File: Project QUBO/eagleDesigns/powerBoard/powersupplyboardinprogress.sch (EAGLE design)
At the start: 12 parts, among them M1 IRF7458PBF, M2 IRF7458PBF

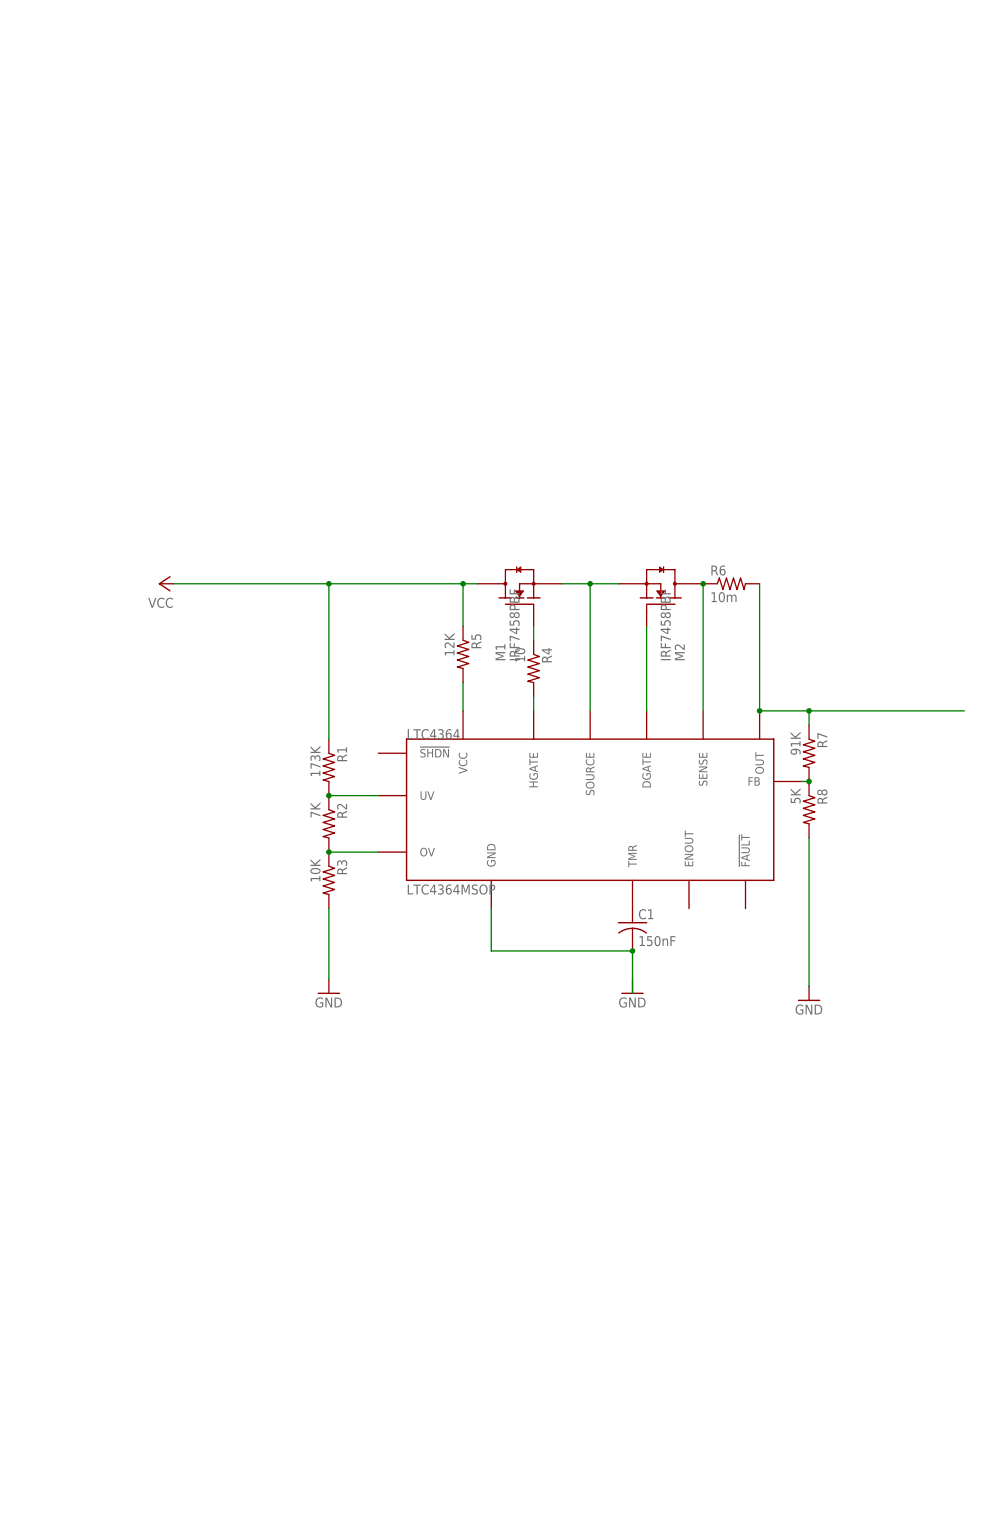
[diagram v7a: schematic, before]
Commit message: 
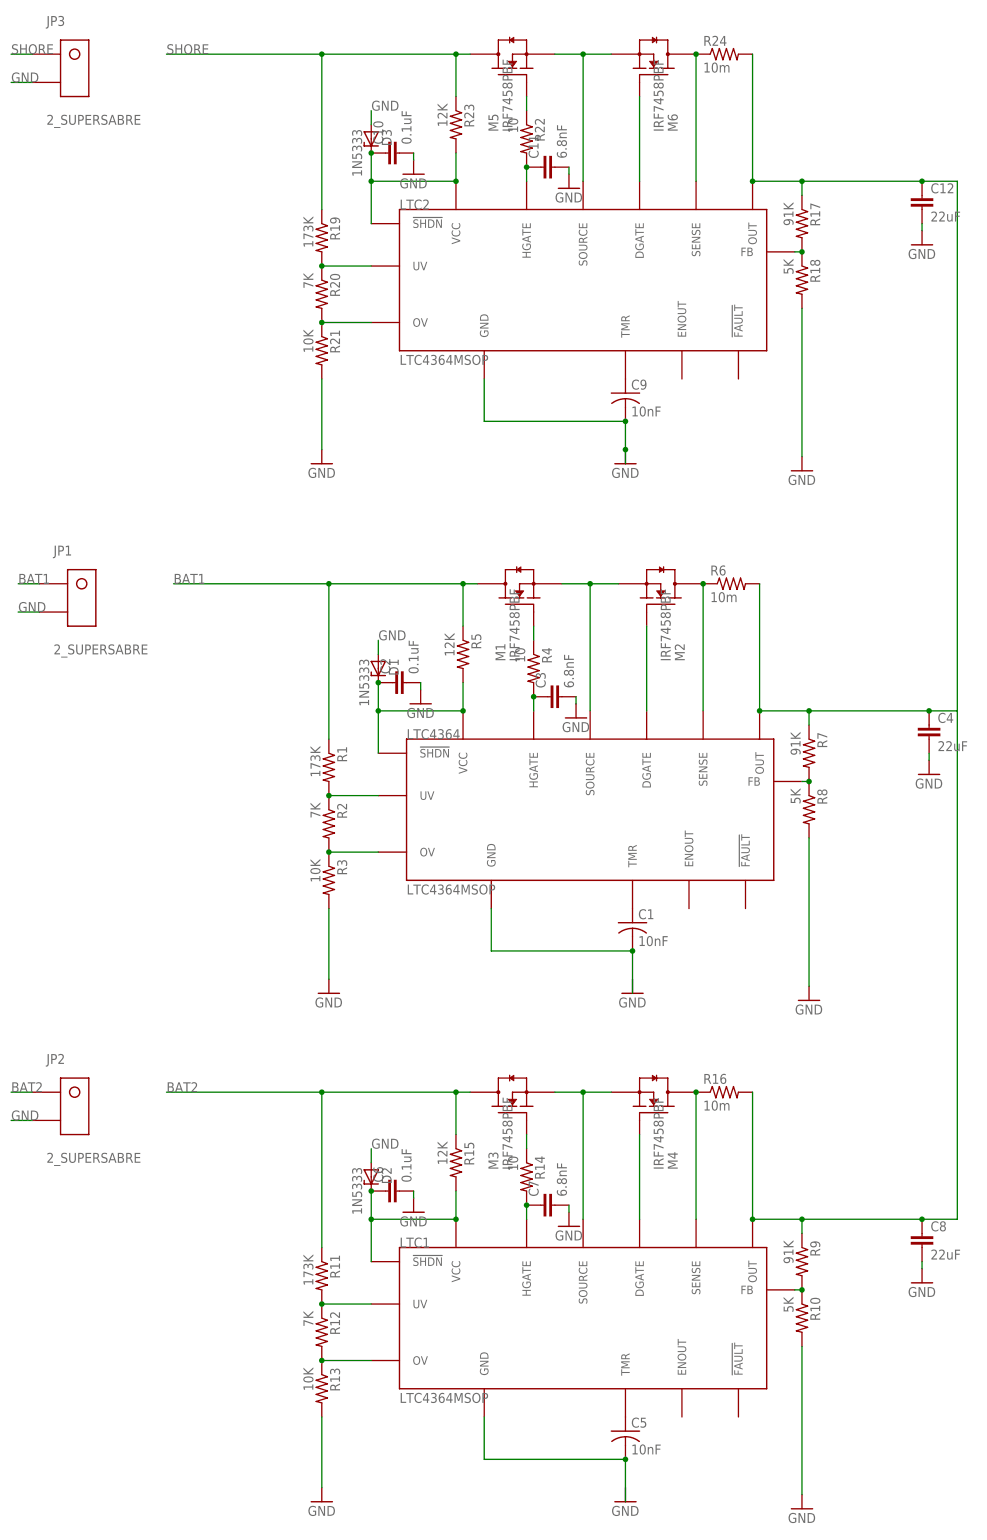
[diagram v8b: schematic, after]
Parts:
- added C10, C2, C6: 0.1uF, resistor:C-EUC0805
- added C11, C3, C7: 6.8nF, resistor:C-EUC0805
- added C12, C4, C8: 22uF, resistor:C-EUC0805
- added C5, C9: 10nF, resistor:C-USC0805
- added D1, D2, D3: 1N5333, diode:1N5333
- added JP1, JP2, JP3: 2_SUPERSABRE, molex:2_SUPERSABRE
- added LTC1, LTC2: LTC4364MSOP, linear:LTC4364MSOP
- added M3, M4, M5, M6: IRF7458PBF, transistor-fet:IRF7458PBF
- added R10, R18: 5K, resistor:R-US_R0805
- added R11, R19: 173K, resistor:R-US_R0805
- added R12, R20: 7K, resistor:R-US_R0805
- added R13, R21: 10K, resistor:R-US_R0805
- added R14, R22: 10, resistor:R-US_R0805
- added R15, R23: 12K, resistor:R-US_R0805
- added R16, R24: 10m, resistor:R-US_R0805
- added R17, R9: 91K, resistor:R-US_R0805
- C1: value 150nF -> 10nF
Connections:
- removed net VCC: M1.D, R1.1, R5.1
- new net BAT1: JP1.P$1, M1.D, R1.1, R5.1
- new net BAT2: JP2.P$1, M3.D, R11.1, R15.1
- new net N$12: C5.1, LTC1.TMR
- new net N$13: LTC1.DGATE, M4.G
- new net N$14: LTC1.SOURCE, M3.S, M4.S
- new net N$15: C12.1, C4.1, C8.1, LTC1.OUT, LTC2.OUT, LTC4364.OUT, R16.2, R17.1, R24.2, R6.2, R7.1, R9.1
- new net N$16: LTC1.FB, R10.1, R9.2
- new net N$17: LTC1.UV, R11.2, R12.1
- new net N$18: LTC1.OV, R12.2, R13.1
- new net N$19: M3.G, R14.1
- new net N$20: C7.1, LTC1.HGATE, R14.2
- new net N$21: C6.1, D2.C, LTC1.!SHDN!, LTC1.VCC, R15.2
- new net N$22: LTC1.SENSE, M4.D, R16.1
- new net N$23: LTC2.DGATE, M6.G
- new net N$24: LTC2.SOURCE, M5.S, M6.S
- new net N$26: LTC2.FB, R17.2, R18.1
- new net N$27: LTC2.UV, R19.2, R20.1
- new net N$28: LTC2.OV, R20.2, R21.1
- new net N$29: M5.G, R22.1
- new net N$30: C11.1, LTC2.HGATE, R22.2
- new net N$31: C10.1, D3.C, LTC2.!SHDN!, LTC2.VCC, R23.2
- new net N$32: LTC2.SENSE, M6.D, R24.1
- new net SHORE: JP3.P$1, M5.D, R19.1, R23.1
- net GND: now also C10.2, C11.2, C12.2, C2.2, C3.2, C4.2, C5.2, C6.2, C7.2, C8.2, C9.2, D1.A, D2.A, D3.A, JP1.P$2, JP2.P$2, JP3.P$2, LTC1.GND, LTC2.GND, R10.2, R13.2, R18.2, R21.2
- net N$10: now also C2.1, D1.C, LTC4364.!SHDN!
- net N$8: now also C3.1
- net N$9: now also C9.1, LTC2.TMR; no longer LTC4364.OUT, R6.2, R7.1
